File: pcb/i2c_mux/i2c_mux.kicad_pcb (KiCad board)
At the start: 2 copper layers, 104.1 x 96.5 mm, 33 parts, among them J1 RJ45, J2 RJ45, J3 RJ45, J4 RJ45, J5 RJ45, J6 RJ45, J7 RJ45, J8 RJ45, J9 RJ45, U1 Adafruit_TCA6548A

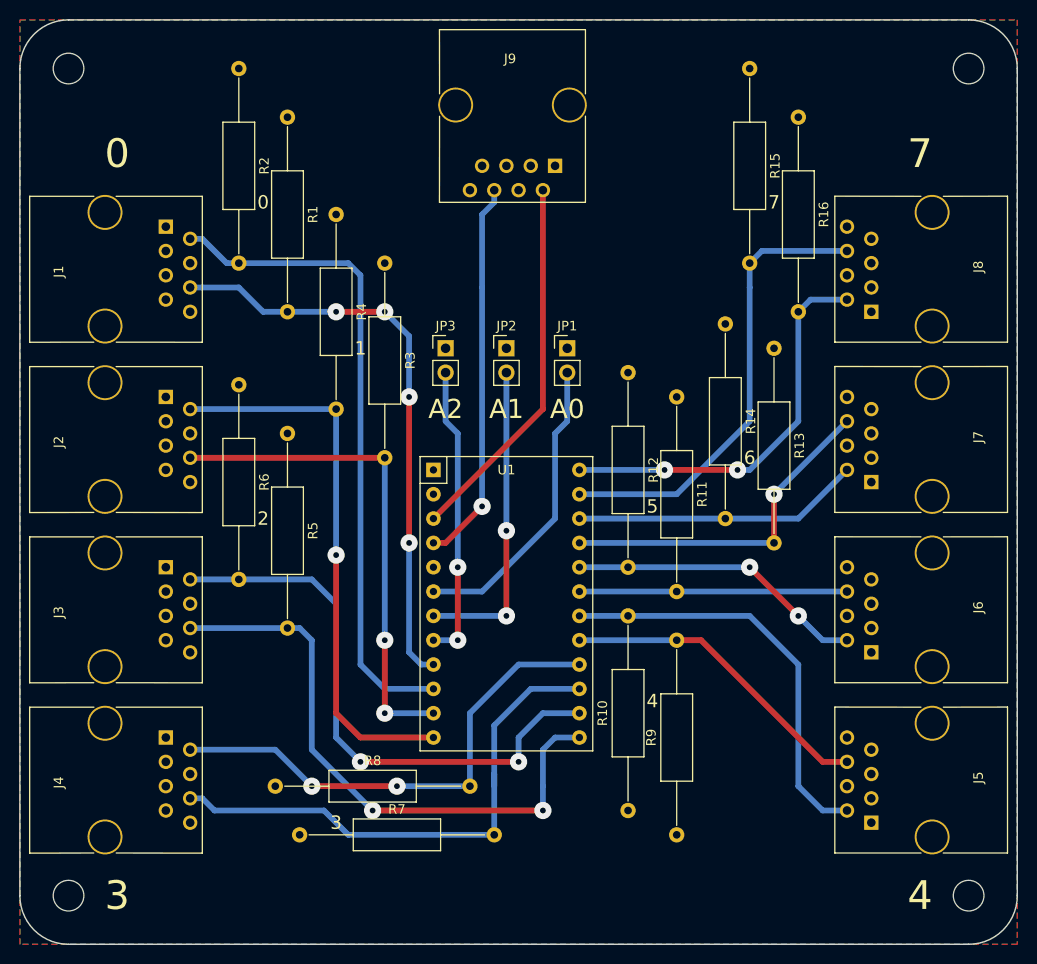
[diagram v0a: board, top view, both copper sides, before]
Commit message: Shorten the multiplexer board to fit 100mm x 100mm
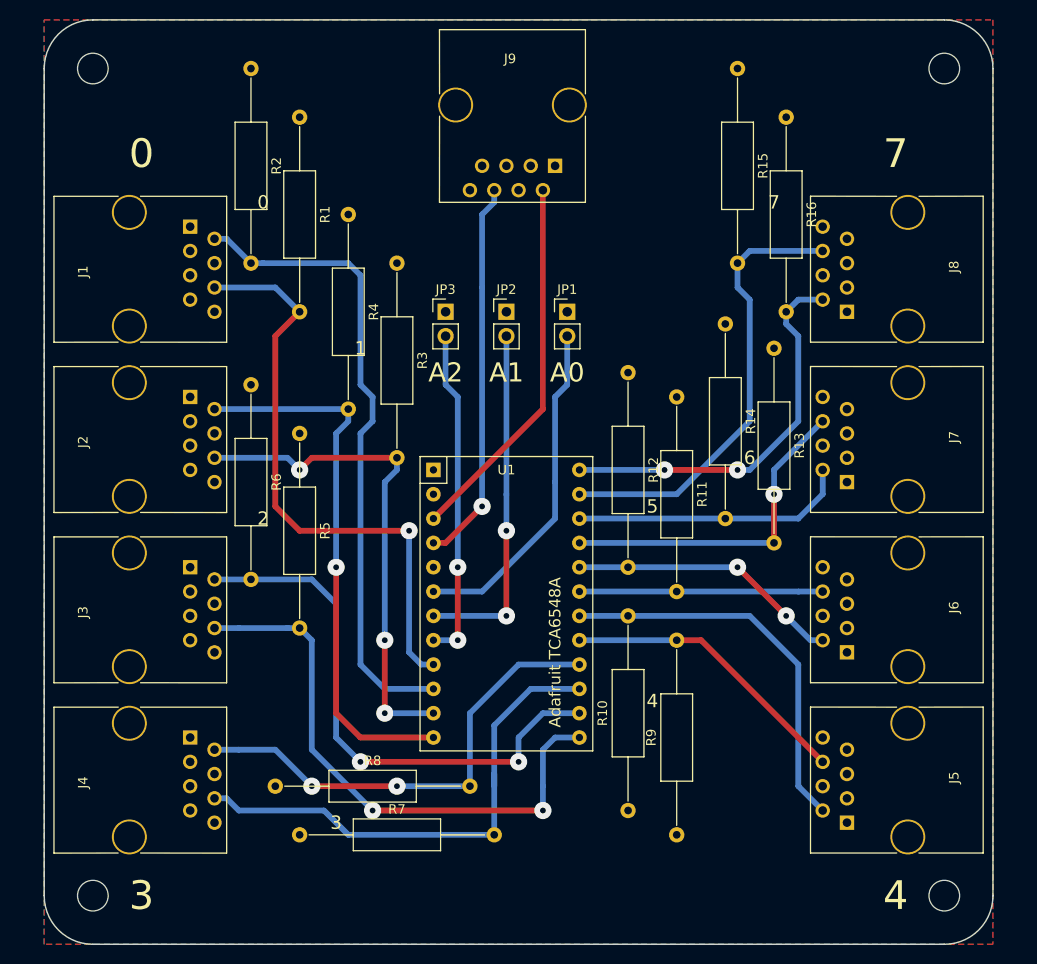
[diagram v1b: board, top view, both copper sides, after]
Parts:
- moved JP1 3.81 mm to (144.8, 80.0)
- moved JP2 3.81 mm to (138.4, 80.0)
- moved JP3 3.81 mm to (132.1, 80.0)
- moved REF** 2.54 mm to (95.2, 141.0)
- moved REF** 2.54 mm to (95.2, 54.6)
- moved J1 2.54 mm to (105.4, 71.1)
- moved J2 2.54 mm to (105.4, 88.9)
- moved J3 2.54 mm to (105.4, 106.7)
- moved J4 2.54 mm to (105.4, 124.5)
- moved J5 2.54 mm to (174.0, 133.3)
- moved J6 2.54 mm to (174.0, 115.6)
- moved J7 2.54 mm to (174.0, 97.8)
- moved J8 2.54 mm to (174.0, 80.0)
- moved REF** 2.54 mm to (184.2, 141.0)
- moved REF** 2.54 mm to (184.2, 54.6)
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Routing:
- net Net-(JP2-Pad2): track 33.0 -> 36.8 mm
- net Net-(JP3-Pad2): track 31.0 -> 34.8 mm
- net Net-(JP1-Pad2): track 31.6 -> 35.4 mm
- net Net-(J6-Pad2): track 31.1 -> 28.6 mm
- net Net-(J6-Pad6): track 27.9 -> 25.4 mm
- net Net-(J5-Pad6): track 33.2 -> 30.7 mm
- net Net-(J5-Pad2): track 43.8 -> 41.3 mm
- net Net-(J4-Pad6): track 56.5 -> 54.0 mm
- net Net-(J4-Pad2): track 51.9 -> 49.4 mm
- net Net-(J3-Pad6): track 62.1 -> 59.6 mm
- net Net-(J3-Pad2): track 60.3 -> 57.8 mm
- net Net-(J1-Pad2): track 68.7 -> 67.2 mm
- net Net-(J7-Pad2): track 30.0 -> 29.0 mm
- net Net-(J7-Pad6): track 36.2 -> 35.1 mm
- net Net-(J1-Pad6): track 61.1 -> 62.1 mm, vias 4 -> 1
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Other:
- board size 104.1 x 96.5 mm -> 99.1 x 96.5 mm
- board text added: "Adafruit TCA6548A"
- board text added: "v1.01 20171114"
- board text removed: "v1.00 20171114"

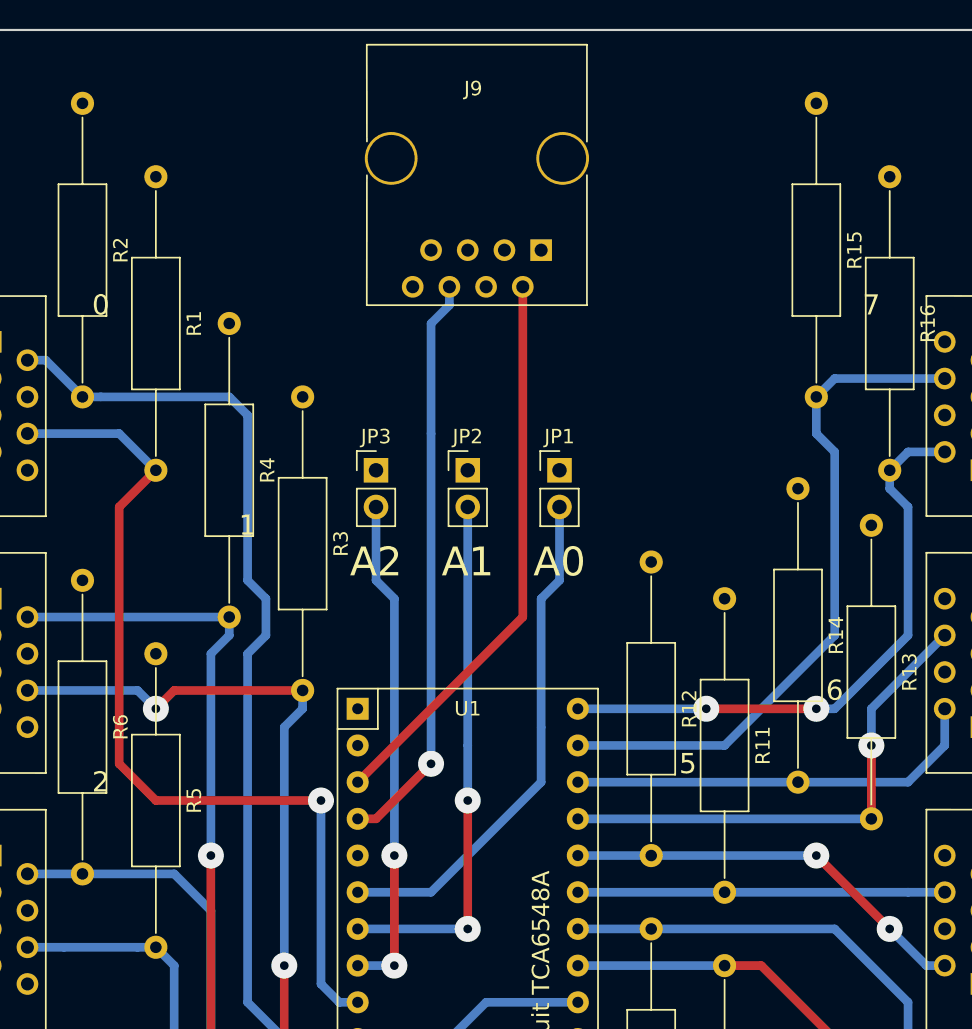
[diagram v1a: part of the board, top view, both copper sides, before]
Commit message: Center the central components (mux v1.02)
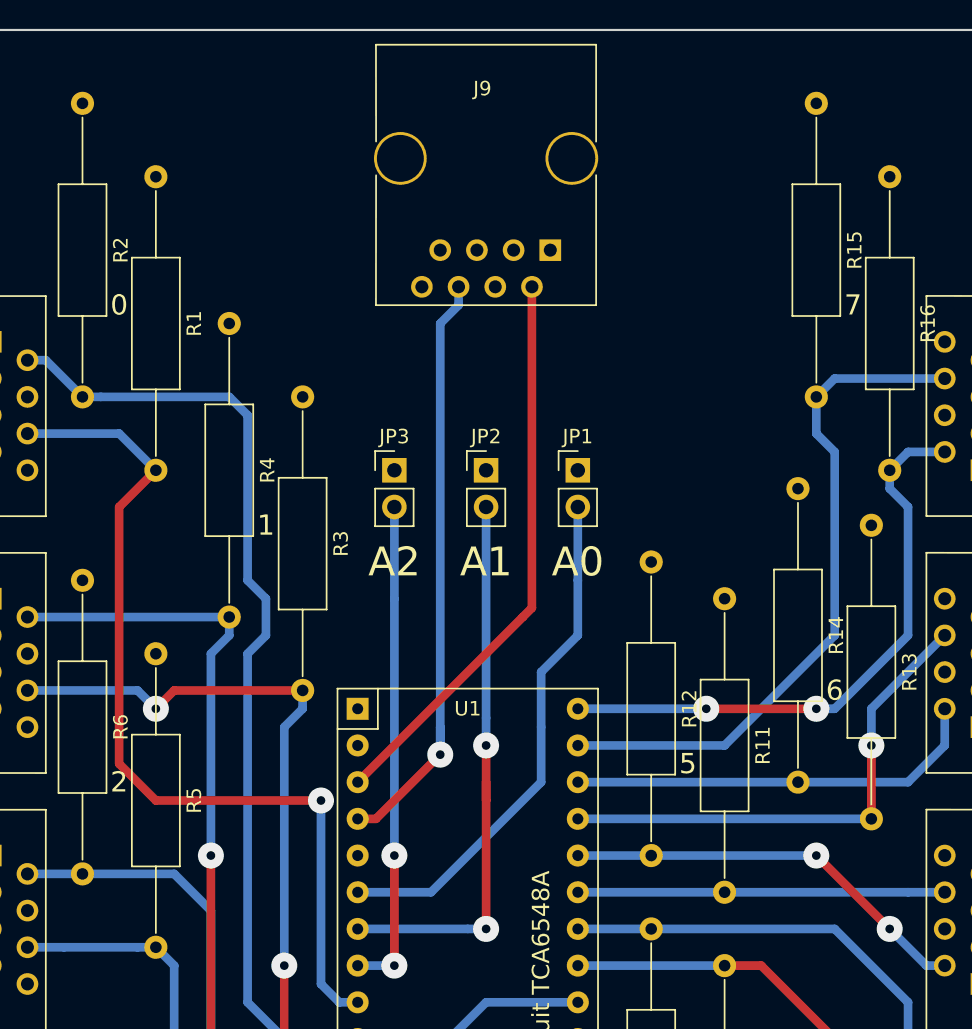
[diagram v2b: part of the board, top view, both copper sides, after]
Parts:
- moved JP1 1.27 mm to (146.1, 80.0)
- moved JP2 1.27 mm to (139.7, 80.0)
- moved JP3 1.27 mm to (133.3, 80.0)
- moved J9 0.64 mm to (144.1, 64.8)
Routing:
- net Net-(JP2-Pad2): track 36.8 -> 39.4 mm
- net Net-(J9-Pad6): track 40.2 -> 42.4 mm
- net Net-(JP1-Pad2): track 35.4 -> 36.0 mm
- net Net-(JP3-Pad2): track 34.8 -> 34.3 mm
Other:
- board text added: "v1.02 20171114"
- board text removed: "v1.01 20171114"
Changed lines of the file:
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@@
     (thickness 1.6)
     (drawings 28)
-    (tracks 163)
+    (tracks 167)
     (zones 0)
     (modules 33)
@@
   )
   (module Connectors:RJ45_8 (layer F.Cu)
-    (at 143.51 64.77 180)
+    (at 144.145 64.77 180)
     (tags RJ45)
     (fp_text reference J9 (at 4.7 11.18 180) (layer F.SilkS)
@@
   )
   (module Pin_Headers:Pin_Header_Straight_1x02_Pitch2.54mm (layer F.Cu)
-    (at 144.78 80.01)
+    (at 146.05 80.01)
     (descr "Through hole straight pin header, 1x02, 2.54mm pitch, single row")
     (tags "Through hole pin header THT 1x02 2.54mm single row")
@@
   )
   (module Pin_Headers:Pin_Header_Straight_1x02_Pitch2.54mm (layer F.Cu)
-    (at 138.43 80.01)
+    (at 139.7 80.01)
     (descr "Through hole straight pin header, 1x02, 2.54mm pitch, single row")
     (tags "Through hole pin header THT 1x02 2.54mm single row")
@@
   )
   (module Pin_Headers:Pin_Header_Straight_1x02_Pitch2.54mm (layer F.Cu)
-    (at 132.08 80.01)
+    (at 133.35 80.01)
     (descr "Through hole straight pin header, 1x02, 2.54mm pitch, single row")
     (tags "Through hole pin header THT 1x02 2.54mm single row")
@@
     (effects (font (size 1.4 1.4) (thickness 0.3)))
   )
-  (gr_text 7 (at 166.37 68.58) (layer F.SilkS)
+  (gr_text 7 (at 165.1 68.58) (layer F.SilkS)
     (effects (font (size 1.4 1.4) (thickness 0.3)))
   )
@@
     (effects (font (size 1.4 1.4) (thickness 0.3)))
   )
-  (gr_text 2 (at 113.03 101.6) (layer F.SilkS)
+  (gr_text 2 (at 114.3 101.6) (layer F.SilkS)
     (effects (font (size 1.4 1.4) (thickness 0.3)))
   )
-  (gr_text 1 (at 123.19 83.82) (layer F.SilkS)
+  (gr_text 1 (at 124.46 83.82) (layer F.SilkS)
     (effects (font (size 1.4 1.4) (thickness 0.3)))
   )
-  (gr_text 0 (at 113.03 68.58) (layer F.SilkS)
+  (gr_text 0 (at 114.3 68.58) (layer F.SilkS)
     (effects (font (size 1.4 1.4) (thickness 0.3)))
   )
-  (gr_text "v1.01 20171114" (at 110.49 140.97) (layer B.SilkS)
+  (gr_text "v1.02 20171114" (at 110.49 140.97) (layer B.SilkS)
     (effects (font (size 1.4 1.4) (thickness 0.3)) (justify mirror))
   )
@@
   (gr_arc (start 184.15 140.97) (end 189.23 140.97) (angle 90) (layer Edge.Cuts) (width 0.15))
   (gr_arc (start 95.25 140.97) (end 95.25 146.05) (angle 90) (layer Edge.Cuts) (width 0.15))
-  (gr_text A2 (at 132.08 86.36) (layer F.SilkS)
+  (gr_text A2 (at 133.35 86.36) (layer F.SilkS)
     (effects (font (size 2 2) (thickness 0.3)))
   )
-  (gr_text A1 (at 138.43 86.36) (layer F.SilkS)
+  (gr_text A1 (at 139.7 86.36) (layer F.SilkS)
     (effects (font (size 2 2) (thickness 0.3)))
   )
-  (gr_text A0 (at 144.78 86.36) (layer F.SilkS)
+  (gr_text A0 (at 146.05 86.36) (layer F.SilkS)
     (effects (font (size 2 2) (thickness 0.3)))
   )
@@
   (segment (start 163.83 91.44) (end 163.83 78.74) (width 0.6) (layer B.Cu) (net 48))
   (segment (start 156.21 99.06) (end 163.83 91.44) (width 0.6) (layer B.Cu) (net 48))
-  (segment (start 142.24 67.31) (end 142.24 90.17) (width 0.6) (layer F.Cu) (net 51))
+  (segment (start 142.875 67.31) (end 142.875 89.535) (width 0.6) (layer F.Cu) (net 51))
+  (segment (start 142.875 89.535) (end 142.24 90.17) (width 0.6) (layer F.Cu) (net 51))
   (segment (start 142.24 90.17) (end 130.81 101.6) (width 0.6) (layer F.Cu) (net 51))
-  (segment (start 137.16 67.31) (end 137.16 68.58) (width 0.6) (layer B.Cu) (net 54))
-  (segment (start 137.16 68.58) (end 135.89 69.85) (width 0.6) (layer B.Cu) (net 54))
-  (segment (start 135.89 77.47) (end 135.89 69.85) (width 0.6) (layer B.Cu) (net 54))
   (segment (start 130.81 104.14) (end 132.08 104.14) (width 0.6) (layer F.Cu) (net 54))
-  (segment (start 135.89 100.33) (end 135.89 77.47) (width 0.6) (layer B.Cu) (net 54))
-  (via (at 135.89 100.33) (size 1.8) (drill 0.6) (layers F.Cu B.Cu) (net 54))
-  (segment (start 132.08 104.14) (end 135.89 100.33) (width 0.6) (layer F.Cu) (net 54))
-  (segment (start 137.16 67.31) (end 137.16 67.31) (width 0.6) (layer B.Cu) (net 54) (status 20))
+  (via (at 136.525 99.695) (size 1.8) (drill 0.6) (layers F.Cu B.Cu) (net 54))
+  (segment (start 132.08 104.14) (end 136.525 99.695) (width 0.6) (layer F.Cu) (net 54))
+  (segment (start 136.525 99.695) (end 136.525 97.79) (width 0.6) (layer B.Cu) (net 54))
+  (segment (start 136.525 69.85) (end 136.525 97.79) (width 0.6) (layer B.Cu) (net 54))
+  (segment (start 136.525 97.79) (end 136.525 99.695) (width 0.6) (layer B.Cu) (net 54))
+  (segment (start 137.795 67.31) (end 137.795 68.58) (width 0.6) (layer B.Cu) (net 54))
+  (segment (start 137.795 68.58) (end 136.525 69.85) (width 0.6) (layer B.Cu) (net 54))
+  (segment (start 146.05 87.63) (end 146.05 91.44) (width 0.6) (layer B.Cu) (net 57))
+  (segment (start 146.05 91.44) (end 143.51 93.98) (width 0.6) (layer B.Cu) (net 57))
   (segment (start 143.51 97.79) (end 143.51 101.6) (width 0.6) (layer B.Cu) (net 57))
+  (segment (start 135.89 109.22) (end 130.81 109.22) (width 0.6) (layer B.Cu) (net 57))
+  (segment (start 143.51 97.79) (end 143.51 93.98) (width 0.6) (layer B.Cu) (net 57))
   (segment (start 135.89 109.22) (end 143.51 101.6) (width 0.6) (layer B.Cu) (net 57))
-  (segment (start 143.51 97.79) (end 143.51 88.9) (width 0.6) (layer B.Cu) (net 57))
-  (segment (start 143.51 88.9) (end 144.78 87.63) (width 0.6) (layer B.Cu) (net 57))
-  (segment (start 144.78 82.55) (end 144.78 87.63) (width 0.6) (layer B.Cu) (net 57))
-  (segment (start 135.89 109.22) (end 130.81 109.22) (width 0.6) (layer B.Cu) (net 57))
-  (segment (start 138.43 99.06) (end 138.43 102.87) (width 0.6) (layer B.Cu) (net 58))
-  (via (at 138.43 102.87) (size 1.8) (drill 0.6) (layers F.Cu B.Cu) (net 58))
-  (segment (start 138.43 102.87) (end 138.43 111.76) (width 0.6) (layer F.Cu) (net 58))
-  (via (at 138.43 111.76) (size 1.8) (drill 0.6) (layers F.Cu B.Cu) (net 58))
+  (segment (start 146.05 82.55) (end 146.05 87.63) (width 0.6) (layer B.Cu) (net 57))
+  (segment (start 139.7 102.87) (end 139.7 99.06) (width 0.6) (layer F.Cu) (net 58))
+  (segment (start 139.7 99.06) (end 139.7 97.155) (width 0.6) (layer B.Cu) (net 58))
+  (via (at 139.7 99.06) (size 1.8) (drill 0.6) (layers F.Cu B.Cu) (net 58))
+  (segment (start 138.43 111.76) (end 139.7 111.76) (width 0.6) (layer B.Cu) (net 58))
+  (segment (start 139.7 111.76) (end 139.7 102.87) (width 0.6) (layer F.Cu) (net 58))
+  (segment (start 139.7 102.87) (end 139.7 101.6) (width 0.6) (layer F.Cu) (net 58))
+  (via (at 139.7 111.76) (size 1.8) (drill 0.6) (layers F.Cu B.Cu) (net 58))
   (segment (start 130.81 111.76) (end 138.43 111.76) (width 0.6) (layer B.Cu) (net 58))
-  (segment (start 138.43 99.06) (end 138.43 82.55) (width 0.6) (layer B.Cu) (net 58))
+  (segment (start 139.7 97.155) (end 139.7 82.55) (width 0.6) (layer B.Cu) (net 58))
+  (segment (start 133.35 82.55) (end 133.35 88.9) (width 0.6) (layer B.Cu) (net 59))
+  (segment (start 133.35 114.3) (end 130.81 114.3) (width 0.6) (layer B.Cu) (net 59))
+  (segment (start 133.35 102.87) (end 133.35 88.9) (width 0.6) (layer B.Cu) (net 59))
+  (via (at 133.35 106.68) (size 1.8) (drill 0.6) (layers F.Cu B.Cu) (net 59))
+  (segment (start 133.35 114.3) (end 133.35 106.68) (width 0.6) (layer F.Cu) (net 59))
+  (via (at 133.35 114.3) (size 1.8) (drill 0.6) (layers F.Cu B.Cu) (net 59))
   (segment (start 133.35 102.87) (end 133.35 106.68) (width 0.6) (layer B.Cu) (net 59))
-  (via (at 133.35 114.3) (size 1.8) (drill 0.6) (layers F.Cu B.Cu) (net 59))
-  (segment (start 133.35 114.3) (end 133.35 106.68) (width 0.6) (layer F.Cu) (net 59))
-  (via (at 133.35 106.68) (size 1.8) (drill 0.6) (layers F.Cu B.Cu) (net 59))
-  (segment (start 133.35 102.87) (end 133.35 88.9) (width 0.6) (layer B.Cu) (net 59))
-  (segment (start 133.35 88.9) (end 132.08 87.63) (width 0.6) (layer B.Cu) (net 59))
-  (segment (start 132.08 82.55) (end 132.08 87.63) (width 0.6) (layer B.Cu) (net 59))
-  (segment (start 133.35 114.3) (end 130.81 114.3) (width 0.6) (layer B.Cu) (net 59))
   (zone (net 1) (net_name GND) (layer B.Cu) (hatch edge 0.508)
     (connect_pads (clearance 0.6))
